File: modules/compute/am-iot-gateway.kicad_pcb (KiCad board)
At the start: 2 copper layers, 22 x 30 mm, 24 parts, among them J1 Bus_M.2_Socket_E, J2 Conn_ARM_SWD_TagConnect_TC203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, SW1 SW_Push, U1 ESP32-C3-MINI-1U-H4

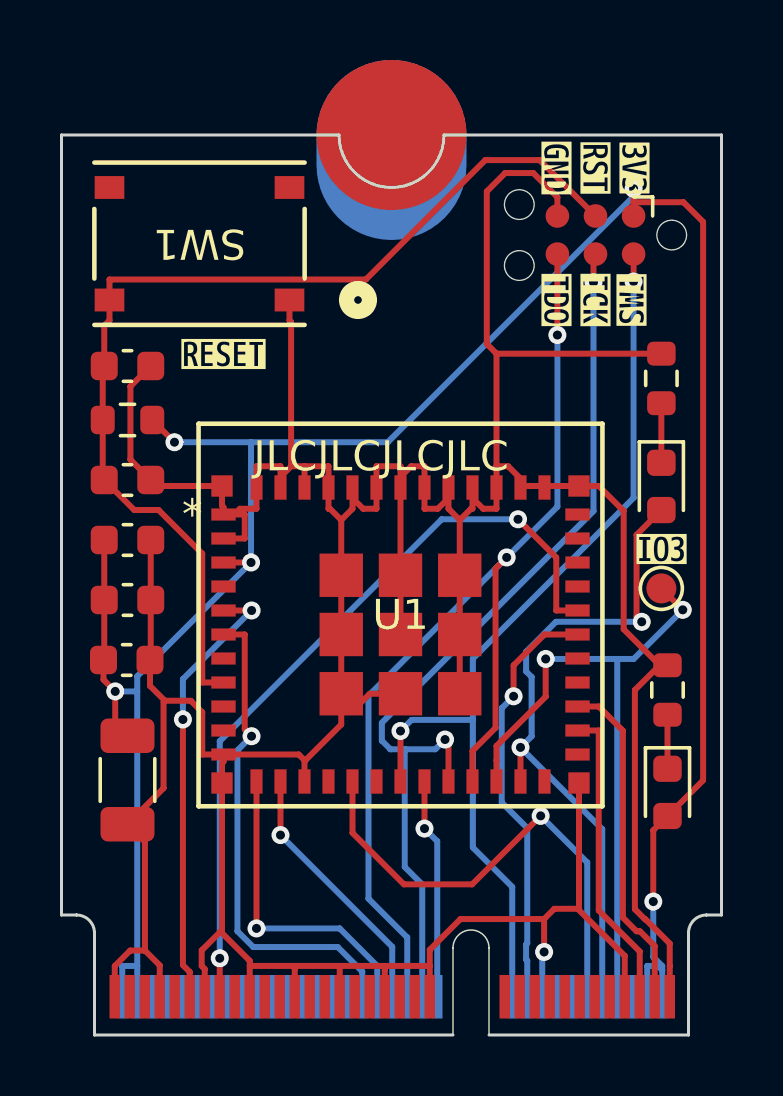
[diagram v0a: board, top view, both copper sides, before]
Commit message: Fix right angled tracks
Signed-off-by: JeffMboya <jangina.mboya@gmail.com>
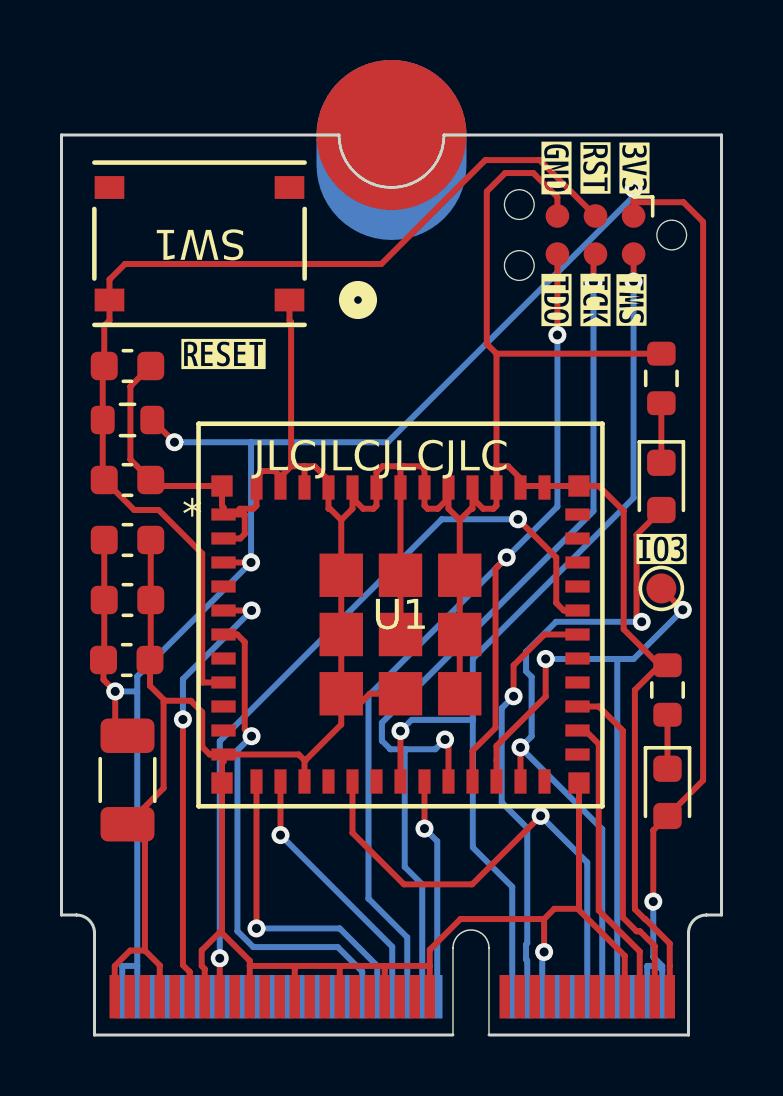
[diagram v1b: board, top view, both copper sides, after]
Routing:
- net GND: track 162.9 -> 161.6 mm
